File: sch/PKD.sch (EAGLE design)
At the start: 28 parts, among them IC1 LM393N, IC3 TL084P, IC4 74HC244N, Q2 BS170

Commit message: BRD update
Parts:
- removed C12: 1n, rcl:C-EU025-025X050
- removed C14: 33n, rcl:C-EU025-025X050
- removed R15: 33, rcl:R-EU_0207/10
- removed R16: 10k, rcl:R-EU_0207/10
- removed R17: 2,2k, rcl:R-EU_0207/10
- added C5: 33n, rcl:C-EU025-025X050
- added C8: 33n, rcl:C-EU050-030X075
- added IC2: TL084P, linear:TL084P
- added JP1: (no value), pinhead:PINHD-1X7
- added R10: 100k, rcl:R-EU_0207/10
- added R11: 33, rcl:R-EU_0207/10
- added R9: 10k, rcl:R-EU_0207/10
- C2: device rcl:C-EU025-025X050 -> rcl:C-EU050-030X075
- C3: value 33n -> 100p
- C6: value 100p -> 1n
- IC3: value TL084P -> PIC12F683P; device linear:TL084P -> microchip:PIC12F683P
- R5: value 510k -> 10k
- R6: value 100k -> 2,2k
- R7: value 10k -> 510k
- renumbered C13 to C7, JP3 to JP2, Q2 to Q1, R14 to R12
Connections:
- removed net PWR_OE2: IC4B.G
- net ANT_LO: now also C6.1; no longer C12.1
- net CROSS_LO: now also JP1.2
- net GND: now also C5.2, C6.2, C8.2, IC2P.V-, IC3.VSS, JP1.3, R7.2; no longer C12.2, C14.2, C3.2, IC3P.V-, R5.2
- net LO_LOAD: now also JP1.7
- net LO_PKD: now also JP1.1, R5.2; no longer R16.2
- net LO_PKD_U: now also C3.2, IC2A.OUT, R10.2, R6.1; no longer C6.2, IC3A.OUT, R17.1, R8.2
- net N$1: now also R7.1; no longer R5.1
- net N$13: now also R11.2; no longer R15.2
- net N$14: now also R11.1; no longer R13.1
- net N$15: now also R13.1; no longer R15.1
- net N$17: now also R5.1, R6.2; no longer R16.1, R17.2
- net N$2: now also IC2A.+IN, R8.1; no longer IC3A.+IN, R6.1
- net N$3: now also IC2B.+IN; no longer IC3B.+IN
- net N$5: now also C3.1, IC2A.-IN, R10.1, R9.2; no longer C6.1, IC3A.-IN, R7.2, R8.1
- net PWR_LO: now also IC3.GP2/AN2/T0CKI/INT/COUT/CCP1, JP1.6
- net PWR_OE1: now also IC4B.G, JP1.5
- net VCC: now also C5.1, C8.1, IC2P.V+, IC3.VDD, JP1.4; no longer C14.1, C3.1, IC3P.V+
- net VMID: now also IC2B.-IN, IC2B.OUT, R8.2, R9.1; no longer IC3B.-IN, IC3B.OUT, R6.2, R7.1
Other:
- moved on the sheet: C3, C4, C6, R13, R5, R6, R7, R8

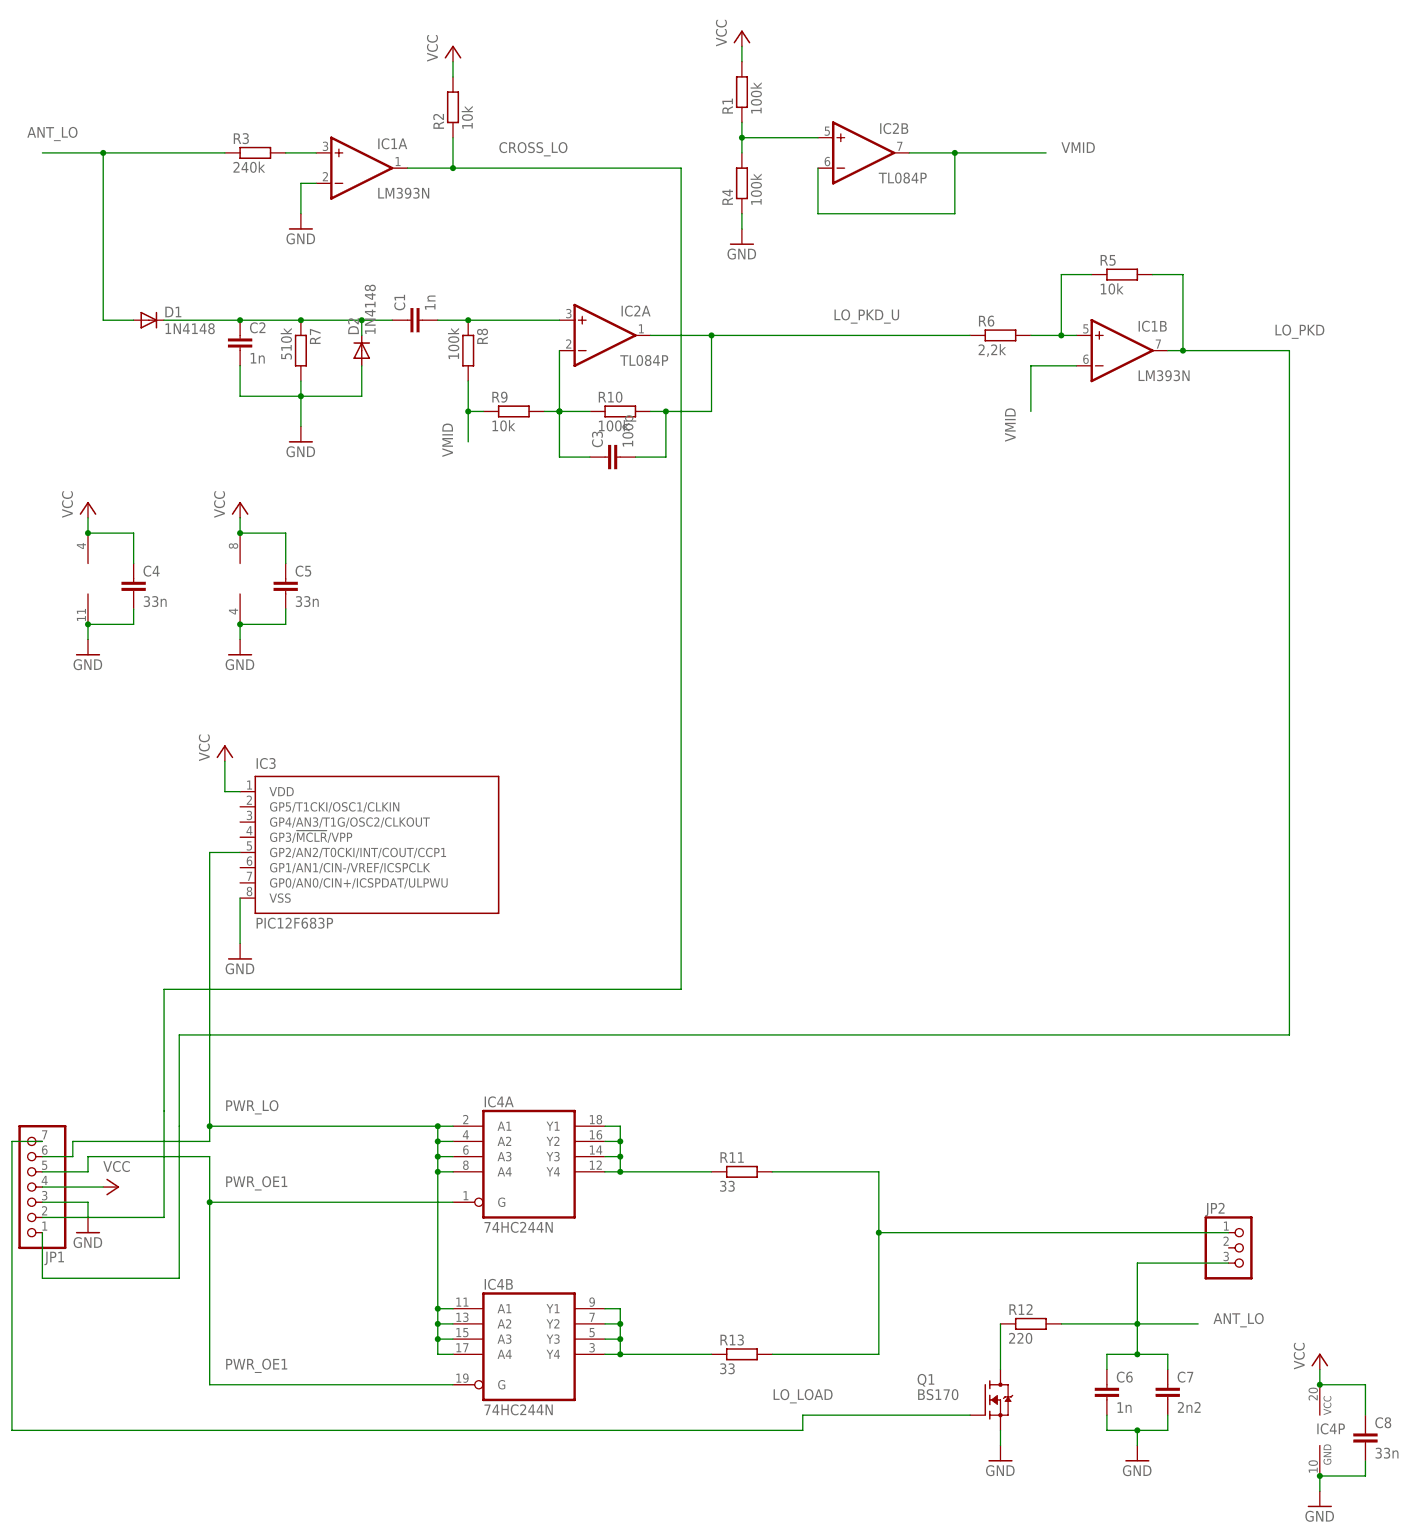
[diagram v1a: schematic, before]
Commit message: Added pic12f firmware and updated schematic
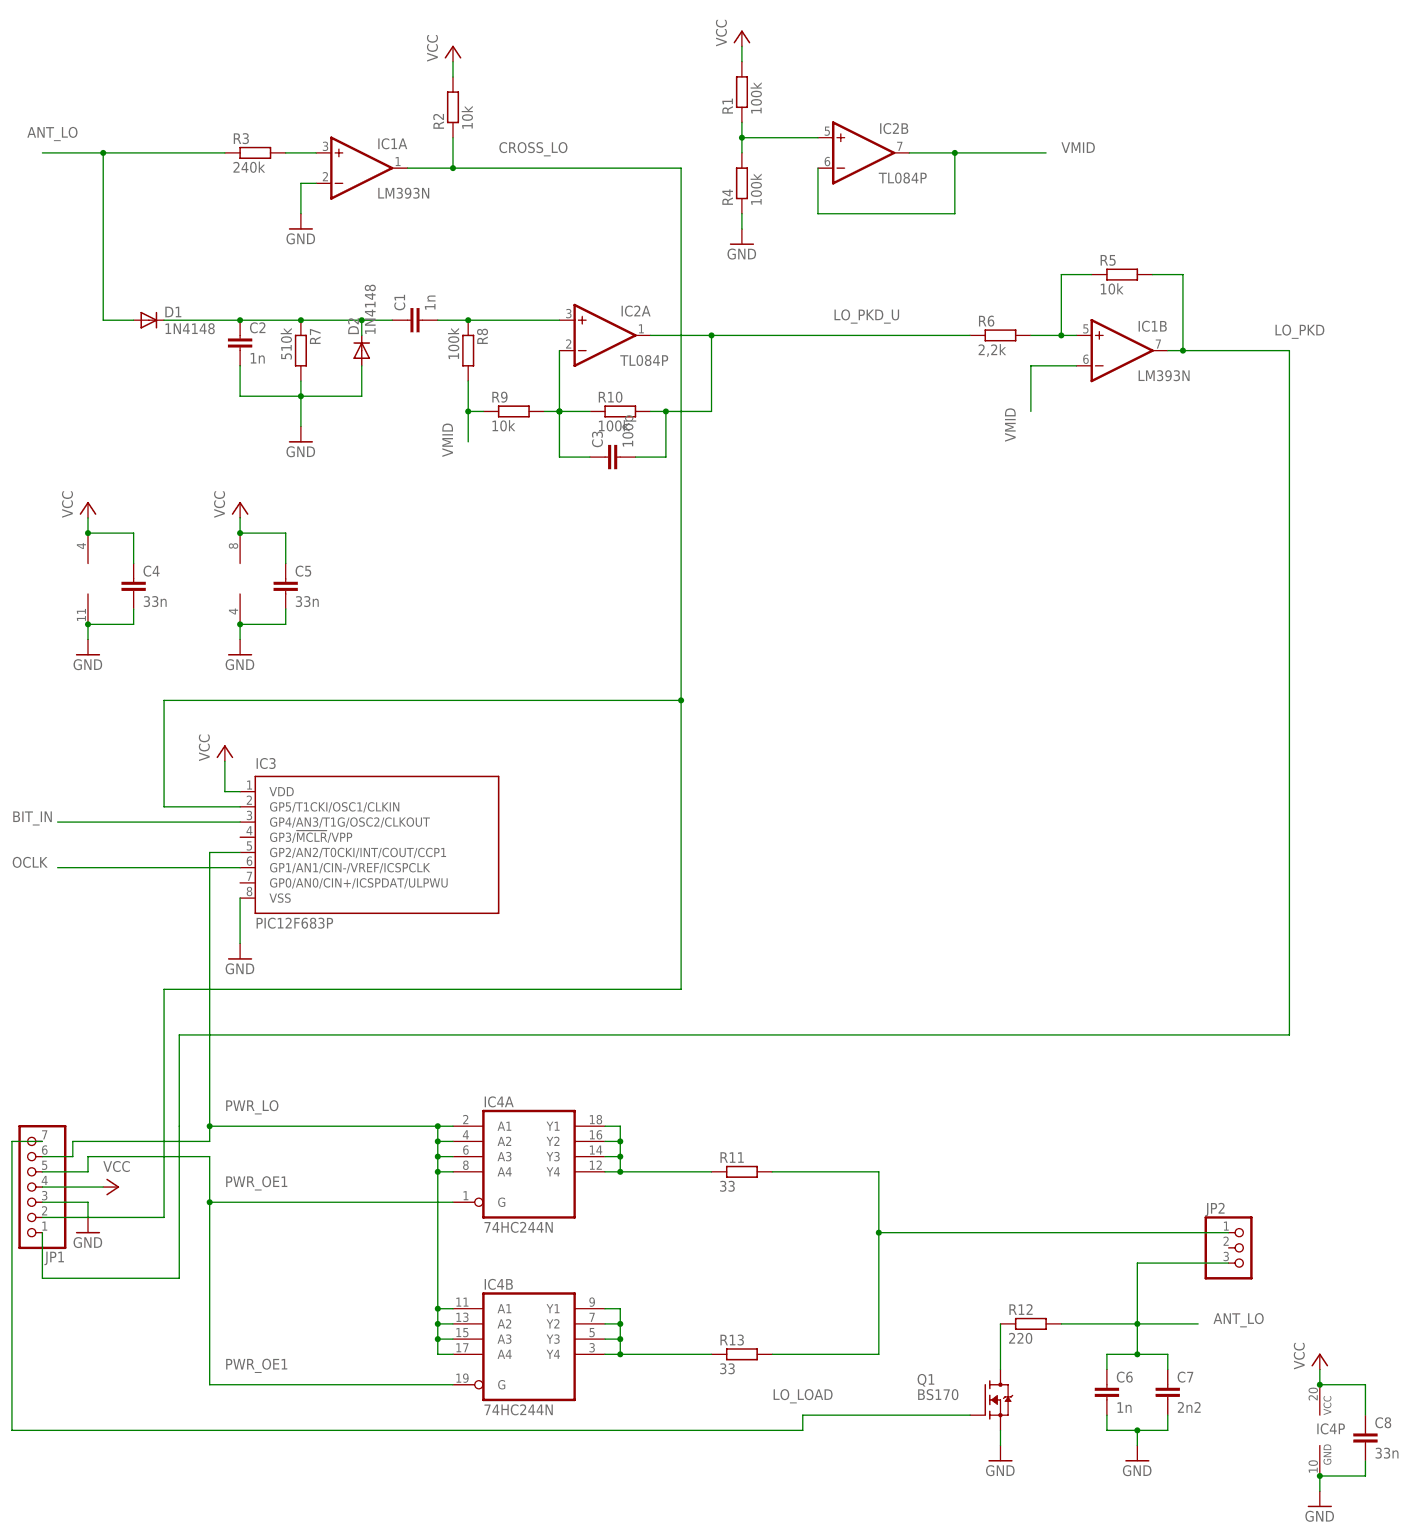
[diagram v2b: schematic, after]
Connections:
- new net BIT_IN: IC3.GP4/AN3/T1G/OSC2/CLKOUT
- new net OCLK: IC3.GP1/AN1/CIN-/VREF/ICSPCLK
- net CROSS_LO: now also IC3.GP5/T1CKI/OSC1/CLKIN
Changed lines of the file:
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@@
 <?xml version="1.0" encoding="utf-8"?>
 <!DOCTYPE eagle SYSTEM "eagle.dtd">
-<eagle version="6.2">
+<eagle version="6.1">
 <drawing>
 <settings>
@@
 <grid distance="0.1" unitdist="inch" unit="inch" style="lines" multiple="1" display="no" altdistance="0.01" altunitdist="inch" altunit="inch"/>
 <layers>
-<layer number="1" name="Top" color="4" fill="1" visible="yes" active="no"/>
-<layer number="16" name="Bottom" color="1" fill="1" visible="yes" active="no"/>
-<layer number="17" name="Pads" color="2" fill="1" visible="yes" active="no"/>
-<layer number="18" name="Vias" color="2" fill="1" visible="yes" active="no"/>
-<layer number="19" name="Unrouted" color="6" fill="1" visible="yes" active="no"/>
-<layer number="20" name="Dimension" color="15" fill="1" visible="yes" active="no"/>
-<layer number="21" name="tPlace" color="7" fill="1" visible="yes" active="no"/>
-<layer number="22" name="bPlace" color="7" fill="1" visible="yes" active="no"/>
-<layer number="23" name="tOrigins" color="15" fill="1" visible="yes" active="no"/>
-<layer number="24" name="bOrigins" color="15" fill="1" visible="yes" active="no"/>
-<layer number="25" name="tNames" color="7" fill="1" visible="yes" active="no"/>
-<layer number="26" name="bNames" color="7" fill="1" visible="yes" active="no"/>
-<layer number="27" name="tValues" color="7" fill="1" visible="yes" active="no"/>
-<layer number="28" name="bValues" color="7" fill="1" visible="yes" active="no"/>
+<layer number="1" name="Top" color="4" fill="1" visible="no" active="no"/>
+<layer number="16" name="Bottom" color="1" fill="1" visible="no" active="no"/>
+<layer number="17" name="Pads" color="2" fill="1" visible="no" active="no"/>
+<layer number="18" name="Vias" color="2" fill="1" visible="no" active="no"/>
+<layer number="19" name="Unrouted" color="6" fill="1" visible="no" active="no"/>
+<layer number="20" name="Dimension" color="15" fill="1" visible="no" active="no"/>
+<layer number="21" name="tPlace" color="7" fill="1" visible="no" active="no"/>
+<layer number="22" name="bPlace" color="7" fill="1" visible="no" active="no"/>
+<layer number="23" name="tOrigins" color="15" fill="1" visible="no" active="no"/>
+<layer number="24" name="bOrigins" color="15" fill="1" visible="no" active="no"/>
+<layer number="25" name="tNames" color="7" fill="1" visible="no" active="no"/>
+<layer number="26" name="bNames" color="7" fill="1" visible="no" active="no"/>
+<layer number="27" name="tValues" color="7" fill="1" visible="no" active="no"/>
+<layer number="28" name="bValues" color="7" fill="1" visible="no" active="no"/>
 <layer number="29" name="tStop" color="7" fill="3" visible="no" active="no"/>
 <layer number="30" name="bStop" color="7" fill="6" visible="no" active="no"/>
@@
 <layer number="35" name="tGlue" color="7" fill="4" visible="no" active="no"/>
 <layer number="36" name="bGlue" color="7" fill="5" visible="no" active="no"/>
-<layer number="37" name="tTest" color="7" fill="1" visible="yes" active="no"/>
-<layer number="38" name="bTest" color="7" fill="1" visible="yes" active="no"/>
+<layer number="37" name="tTest" color="7" fill="1" visible="no" active="no"/>
+<layer number="38" name="bTest" color="7" fill="1" visible="no" active="no"/>
 <layer number="39" name="tKeepout" color="4" fill="11" visible="no" active="no"/>
 <layer number="40" name="bKeepout" color="1" fill="11" visible="no" active="no"/>
@@
 <layer number="44" name="Drills" color="7" fill="1" visible="no" active="no"/>
 <layer number="45" name="Holes" color="7" fill="1" visible="no" active="no"/>
-<layer number="46" name="Milling" color="3" fill="1" visible="yes" active="no"/>
-<layer number="47" name="Measures" color="7" fill="1" visible="yes" active="no"/>
-<layer number="48" name="Document" color="7" fill="1" visible="yes" active="no"/>
-<layer number="49" name="Reference" color="7" fill="1" visible="yes" active="no"/>
-<layer number="51" name="tDocu" color="7" fill="1" visible="yes" active="no"/>
-<layer number="52" name="bDocu" color="7" fill="1" visible="yes" active="no"/>
+<layer number="46" name="Milling" color="3" fill="1" visible="no" active="no"/>
+<layer number="47" name="Measures" color="7" fill="1" visible="no" active="no"/>
+<layer number="48" name="Document" color="7" fill="1" visible="no" active="no"/>
+<layer number="49" name="Reference" color="7" fill="1" visible="no" active="no"/>
+<layer number="51" name="tDocu" color="7" fill="1" visible="no" active="no"/>
+<layer number="52" name="bDocu" color="7" fill="1" visible="no" active="no"/>
 <layer number="91" name="Nets" color="2" fill="1" visible="yes" active="yes"/>
 <layer number="92" name="Busses" color="1" fill="1" visible="yes" active="yes"/>
@@
 <pinref part="R2" gate="G$1" pin="1"/>
 <wire x1="76.2" y1="233.68" x2="114.3" y2="233.68" width="0.1524" layer="91"/>
-<wire x1="114.3" y1="233.68" x2="114.3" y2="96.52" width="0.1524" layer="91"/>
+<wire x1="114.3" y1="233.68" x2="114.3" y2="144.78" width="0.1524" layer="91"/>
+<wire x1="114.3" y1="144.78" x2="114.3" y2="96.52" width="0.1524" layer="91"/>
 <wire x1="114.3" y1="96.52" x2="27.94" y2="96.52" width="0.1524" layer="91"/>
-<wire x1="27.94" y1="96.52" x2="27.94" y2="76.2" width="0.1524" layer="91"/>
-<wire x1="27.94" y1="76.2" x2="27.94" y2="58.42" width="0.1524" layer="91"/>
+<wire x1="27.94" y1="96.52" x2="27.94" y2="58.42" width="0.1524" layer="91"/>
 <pinref part="JP1" gate="A" pin="2"/>
 <wire x1="27.94" y1="58.42" x2="7.62" y2="58.42" width="0.1524" layer="91"/>
+<pinref part="IC3" gate="G$1" pin="GP5/T1CKI/OSC1/CLKIN"/>
+<wire x1="40.64" y1="127" x2="27.94" y2="127" width="0.1524" layer="91"/>
+<wire x1="27.94" y1="127" x2="27.94" y2="144.78" width="0.1524" layer="91"/>
+<wire x1="27.94" y1="144.78" x2="114.3" y2="144.78" width="0.1524" layer="91"/>
+<junction x="114.3" y="144.78"/>
 </segment>
 </net>
@@
 </segment>
 </net>
+<net name="OCLK" class="0">
+<segment>
+<pinref part="IC3" gate="G$1" pin="GP1/AN1/CIN-/VREF/ICSPCLK"/>
+<wire x1="40.64" y1="116.84" x2="10.16" y2="116.84" width="0.1524" layer="91"/>
+<label x="2.54" y="116.84" size="1.778" layer="95"/>
+</segment>
+</net>
+<net name="BIT_IN" class="0">
+<segment>
+<pinref part="IC3" gate="G$1" pin="GP4/AN3/T1G/OSC2/CLKOUT"/>
+<wire x1="40.64" y1="124.46" x2="10.16" y2="124.46" width="0.1524" layer="91"/>
+<label x="2.54" y="124.46" size="1.778" layer="95"/>
+</segment>
+</net>

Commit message: First emulator function - not working
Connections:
- new net NRST: IC3.GP3/!MCLR!/VPP
- new net R/E: IC3.GP0/AN0/CIN+/ICSPDAT/ULPWU
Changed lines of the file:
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@@
+</segment>
+</net>
+<net name="R/E" class="0">
+<segment>
+<pinref part="IC3" gate="G$1" pin="GP0/AN0/CIN+/ICSPDAT/ULPWU"/>
+<wire x1="40.64" y1="114.3" x2="10.16" y2="114.3" width="0.1524" layer="91"/>
+<label x="2.54" y="114.3" size="1.778" layer="95"/>
+</segment>
+</net>
+<net name="NRST" class="0">
+<segment>
+<pinref part="IC3" gate="G$1" pin="GP3/!MCLR!/VPP"/>
+<wire x1="40.64" y1="121.92" x2="10.16" y2="121.92" width="0.1524" layer="91"/>
+<label x="2.54" y="121.92" size="1.778" layer="95"/>
 </segment>
 </net>
